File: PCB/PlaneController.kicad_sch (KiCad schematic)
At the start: 14 parts, among them J1 Conn_01x06_Pin, J2 Conn_01x04_Pin, J3 Conn_01x03, J4 Conn_02x04_Odd_Even, M1 Motor_Servo, M2 Motor_Servo, M3 Motor_Servo, M4 Motor_Servo, M5 Motor_Servo

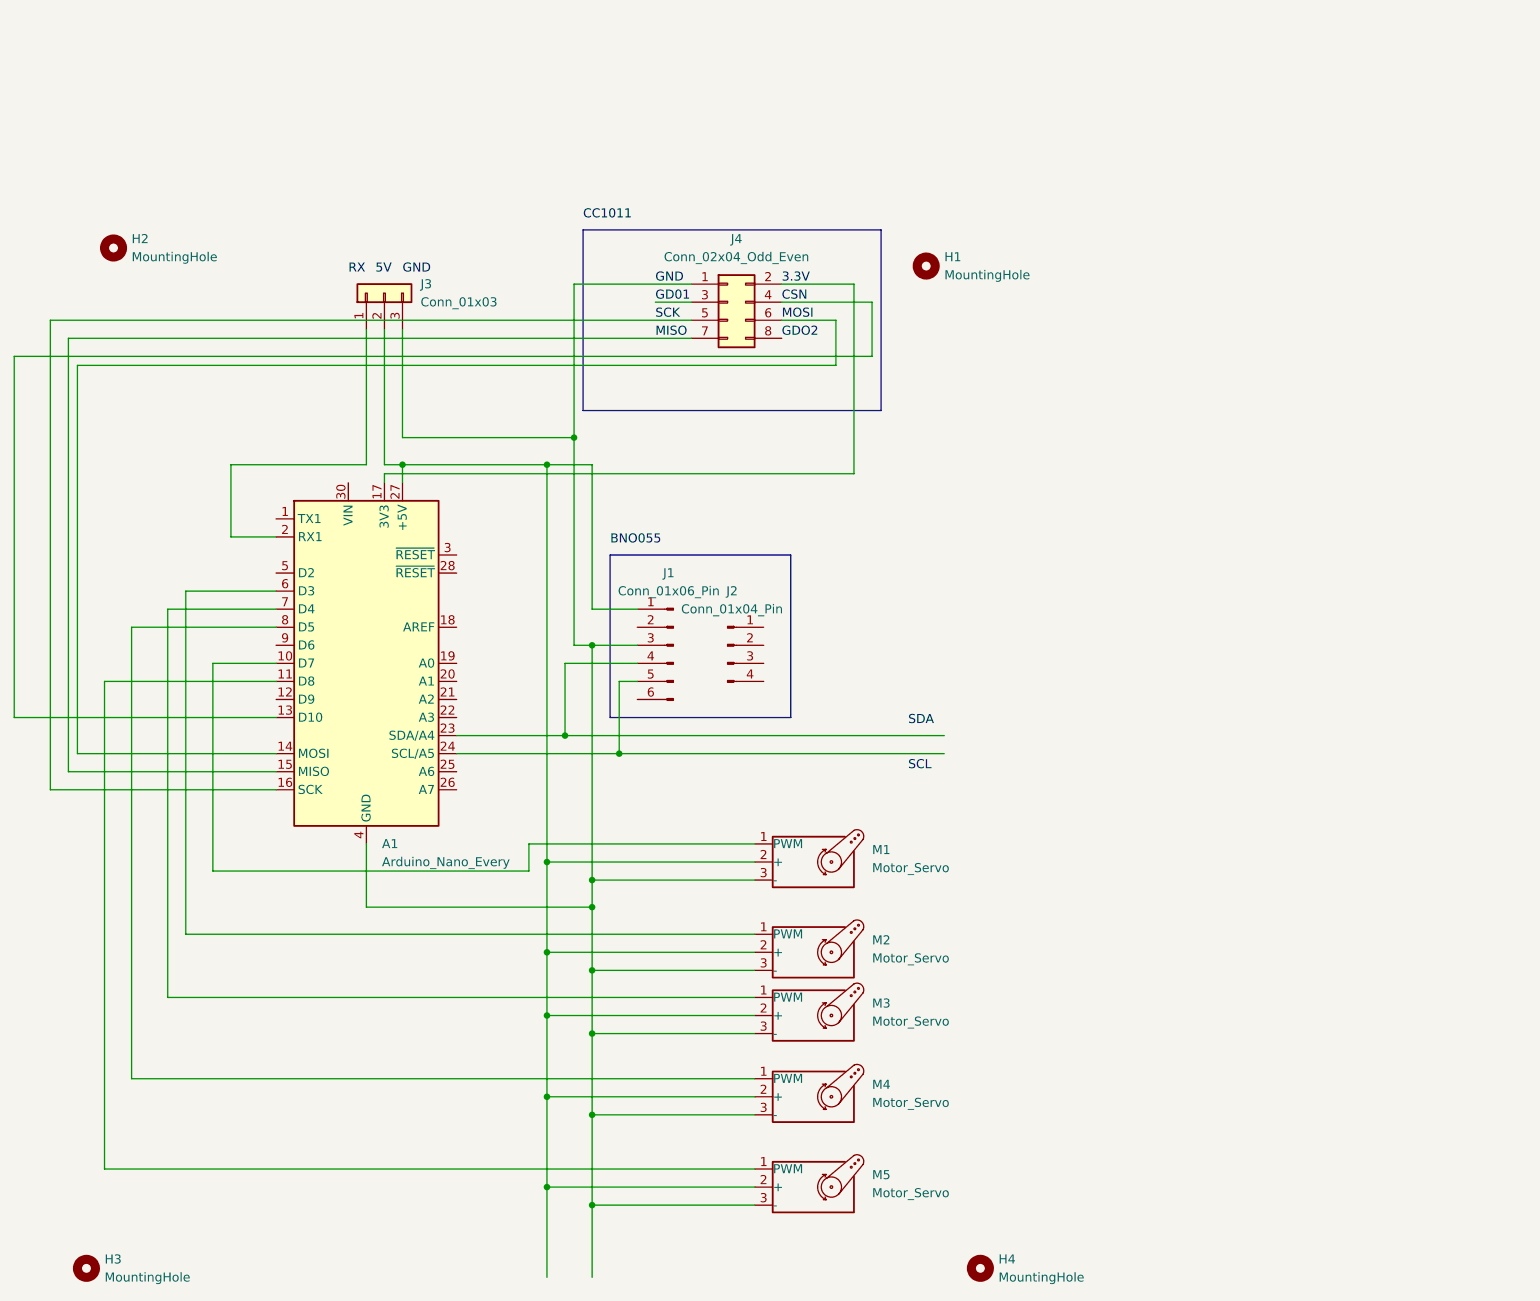
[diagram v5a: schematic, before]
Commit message: Add 3 more GPIO pins to the main PCB
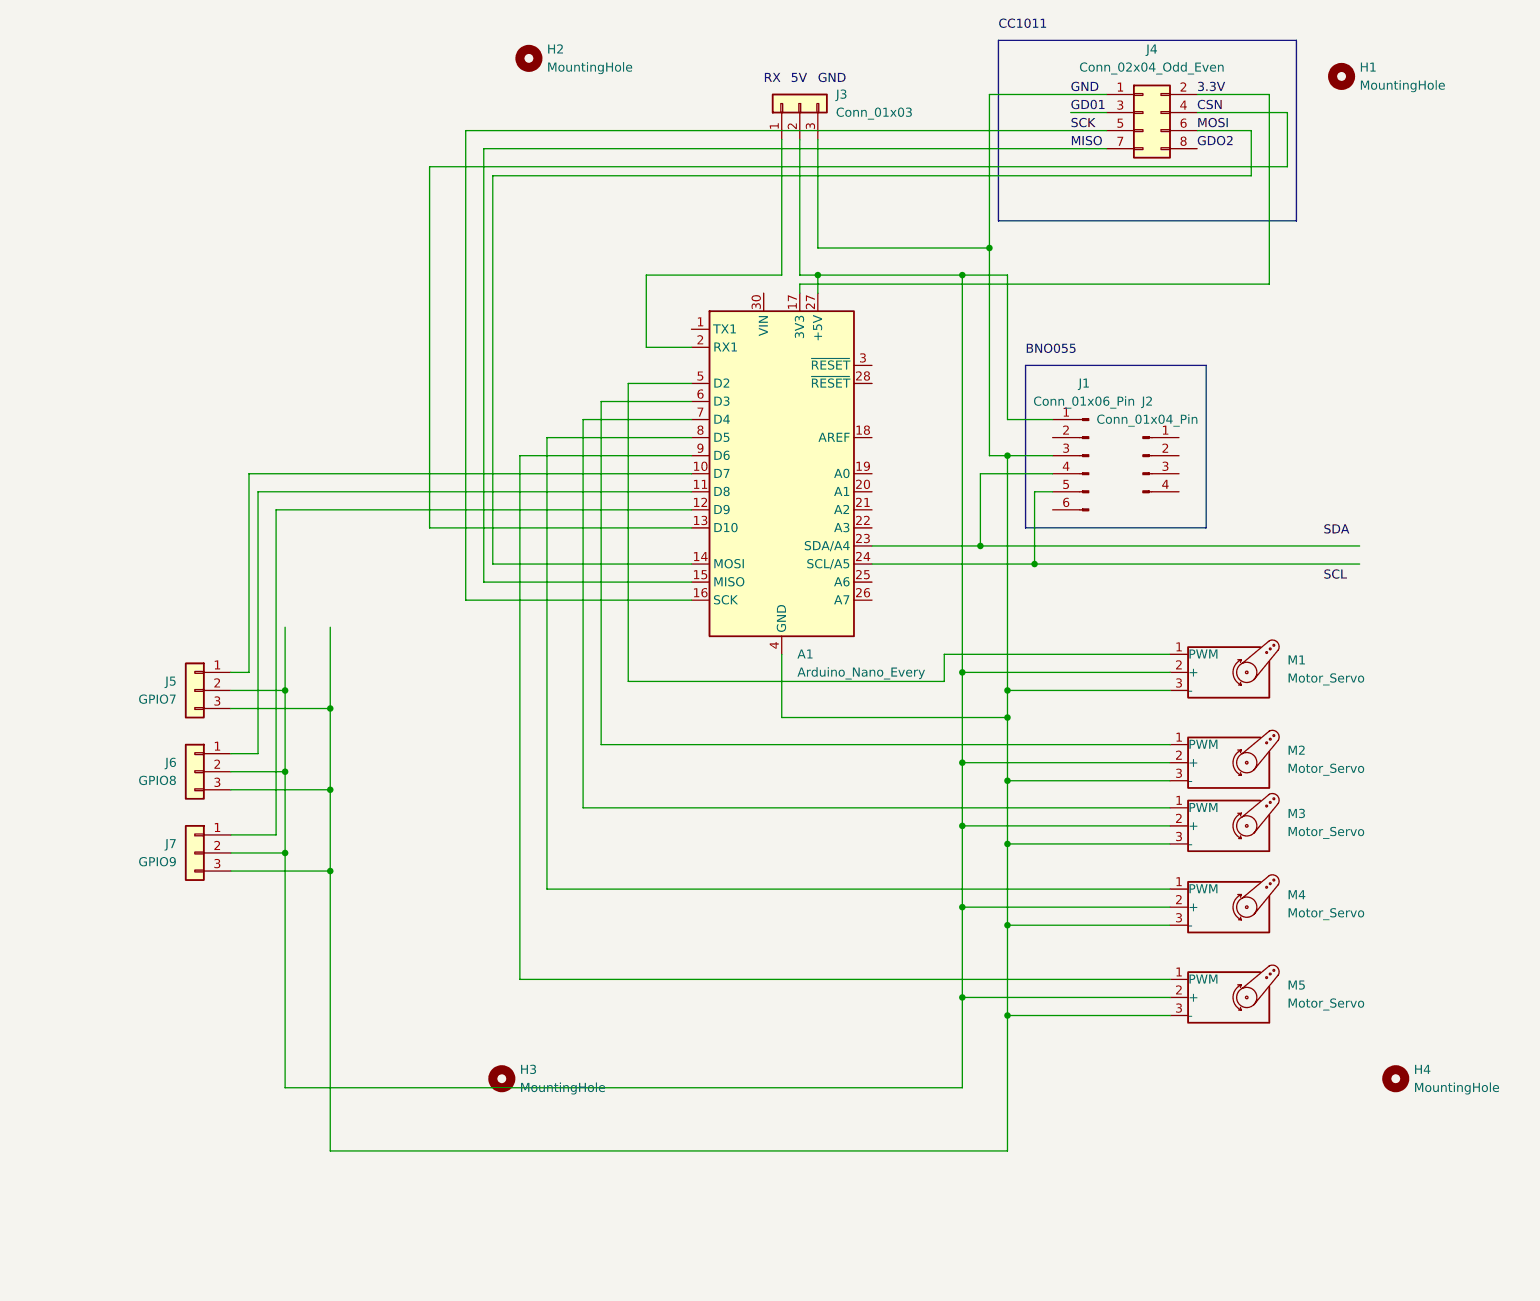
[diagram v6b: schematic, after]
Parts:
- added J5: GPIO7, Connector_PinHeader_2.54mm:PinHeader_1x03_P2.54mm_Vertical, symbol Connector_Generic:Conn_01x03
- added J6: GPIO8, Connector_PinHeader_2.54mm:PinHeader_1x03_P2.54mm_Vertical, symbol Connector_Generic:Conn_01x03
- added J7: GPIO9, Connector_PinHeader_2.54mm:PinHeader_1x03_P2.54mm_Vertical, symbol Connector_Generic:Conn_01x03
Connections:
- net GND: now also J5.3 (Pin_3), J6.3 (Pin_3), J7.3 (Pin_3)
- net at A1.27 (+5V), J1.1 (Pin_1), J3.2 (Pin_2)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: now also J5.2 (Pin_2), J6.2 (Pin_2), J7.2 (Pin_2)
- net at A1.11 (D8): now also J6.1 (Pin_1); no longer M5.1 (PWM)
- net at A1.10 (D7): now also J5.1 (Pin_1); no longer M1.1 (PWM)
- net at A1.12 (D9): now also J7.1 (Pin_1)
- net at A1.5 (D2): now also M1.1 (PWM)
- net at A1.9 (D6): now also M5.1 (PWM)
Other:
- moved on the sheet: A1, H1, H2, H3, H4, J1, J2, J3, J4, M1, M2, M3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
